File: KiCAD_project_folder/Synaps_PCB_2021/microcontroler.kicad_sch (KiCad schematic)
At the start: 27 parts, among them IC2 ESP32-S2, Y2 Crystal_GND24

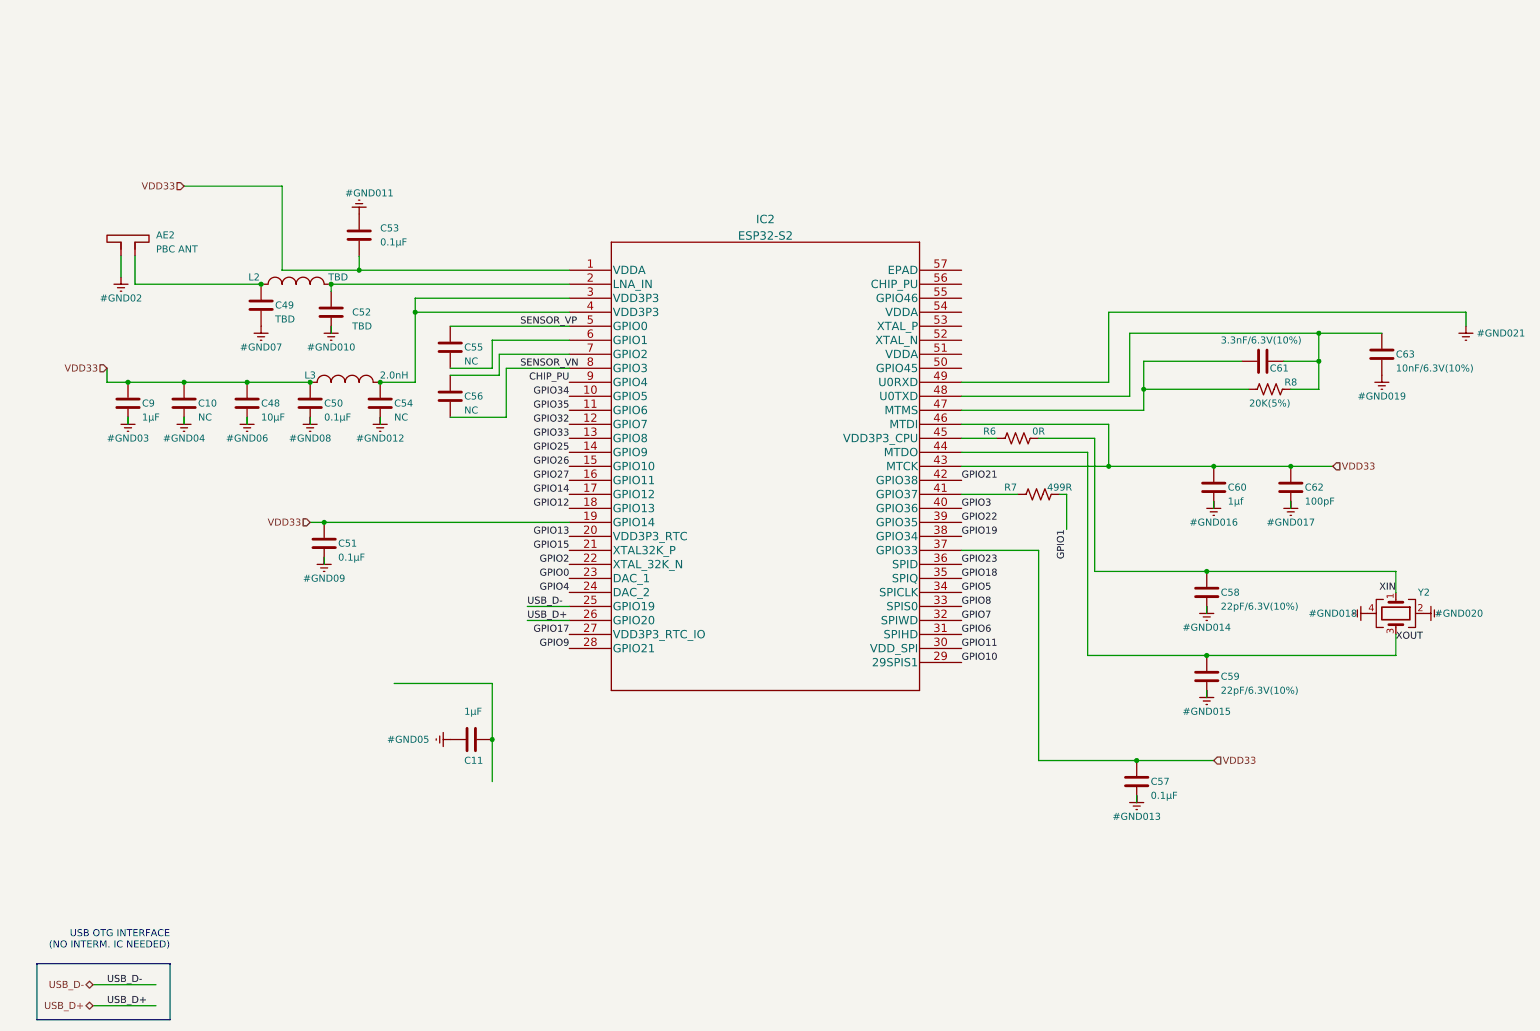
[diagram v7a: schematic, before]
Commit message: Redid schematic, fixed wrong setup
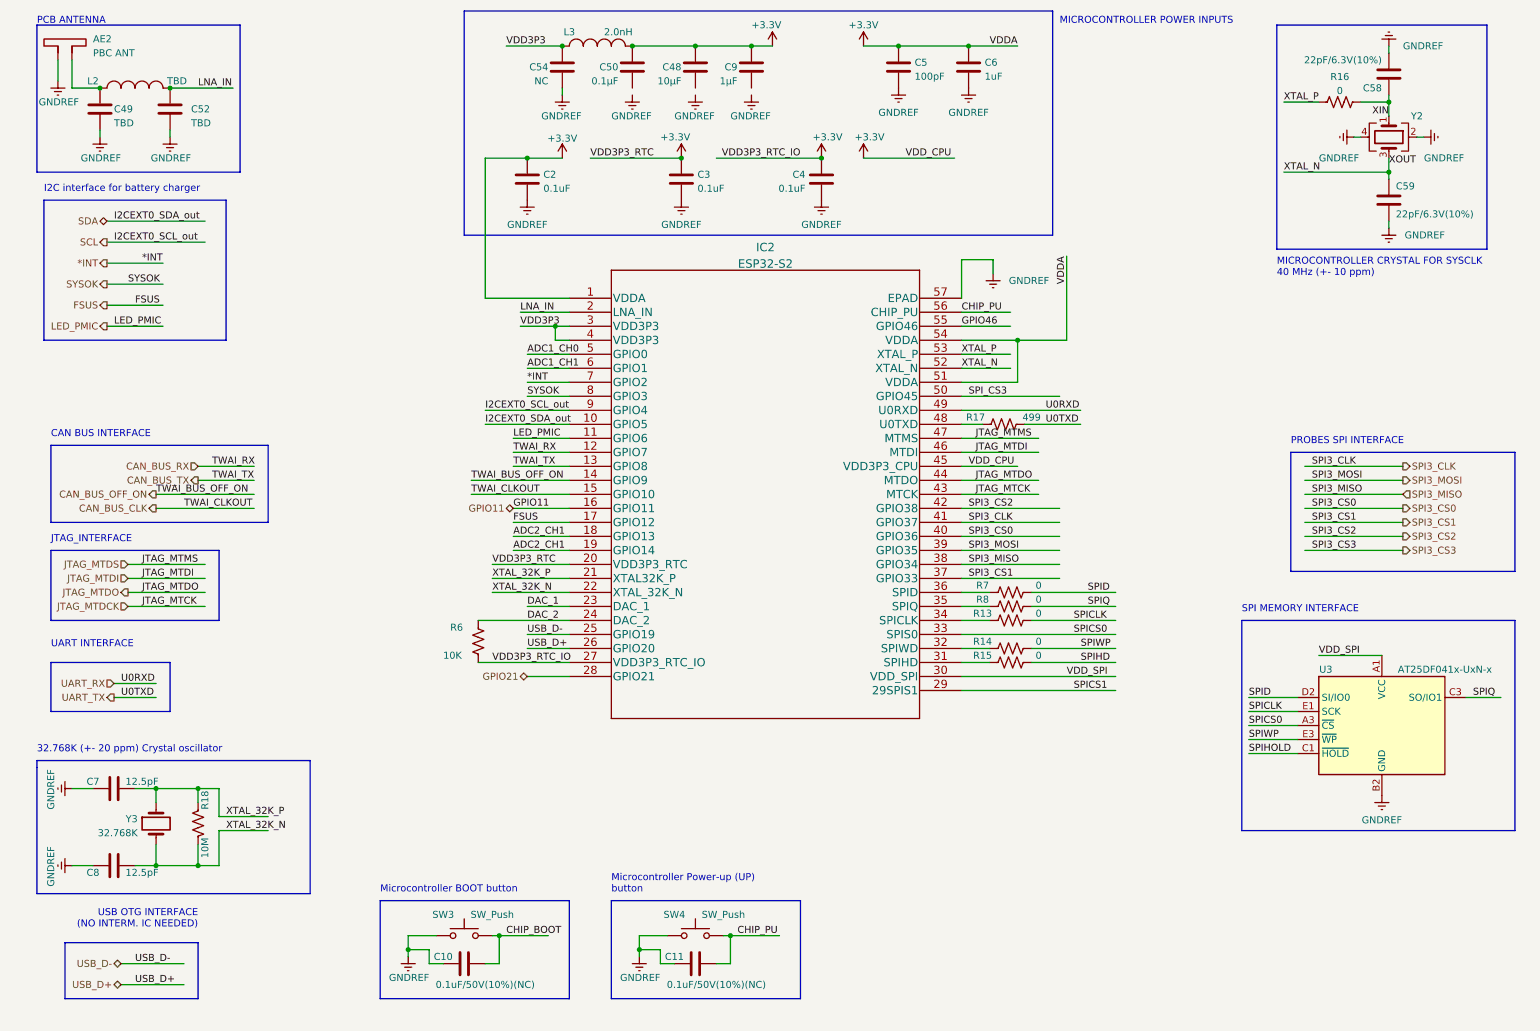
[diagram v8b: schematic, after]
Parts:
- removed C51, C53, C57: 0.1µF, Capacitor_SMD:C_1206_3216Metric_Pad1.33x1.80mm_HandSolder, symbol Device:C
- removed C55, C56: NC, Capacitor_SMD:C_1206_3216Metric_Pad1.33x1.80mm_HandSolder, symbol Device:C
- removed C60: 1µf, Capacitor_SMD:C_1206_3216Metric_Pad1.33x1.80mm_HandSolder, symbol Device:C
- removed C61: 3.3nF/6.3V(10%), Capacitor_SMD:C_1206_3216Metric_Pad1.33x1.80mm_HandSolder, symbol Device:C
- removed C62: 100pF, Capacitor_SMD:C_1206_3216Metric_Pad1.33x1.80mm_HandSolder, symbol Device:C
- removed C63: 10nF/6.3V(10%), Capacitor_SMD:C_1206_3216Metric_Pad1.33x1.80mm_HandSolder, symbol Device:C
- added C2, C3, C4: 0.1uF, symbol Device:C
- added C5: 100pF, symbol Device:C
- added C6: 1uF, symbol Device:C
- added C7, C8: 12.5pF, symbol Device:C
- added R13, R14, R15, R16: 0, symbol Device:R_US
- added R17: 499, symbol Device:R_US
- added R18: 10M, symbol Device:R_US
- added SW3, SW4: SW_Push, symbol Switch:SW_Push
- added U3: AT25DF041x-UxN-x, Package_CSP:WLCSP-8_1.58x1.63x0.35mm_Layout3x5_P0.35x0.4mm_Ball0.25mm_Pad0.25mm_NSMD, symbol Memory_Flash:AT25DF041x-UxN-x
- added Y3: 32.768K, symbol Device:Crystal
- C10: value NC -> 0.1uF/50V(10%)(NC); footprint Capacitor_SMD:C_1206_3216Metric_Pad1.33x1.80mm_HandSolder -> (none)
- C11: value 1µF -> 0.1uF/50V(10%)(NC); footprint Capacitor_SMD:C_1206_3216Metric_Pad1.33x1.80mm_HandSolder -> (none)
- R6: value 0R -> 10K; footprint Resistor_SMD:R_1206_3216Metric_Pad1.30x1.75mm_HandSolder -> (none)
- R7: value 499R -> 0; footprint Resistor_SMD:R_1206_3216Metric_Pad1.30x1.75mm_HandSolder -> (none)
- R8: value 20K(5%) -> 0; footprint Resistor_SMD:R_1206_3216Metric_Pad1.30x1.75mm_HandSolder -> (none)
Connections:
- net GPIO13 is gone; now on net +3V3: IC2.20 (VDD3P3_RTC)
- net GPIO17 is gone; now on net +3V3: IC2.27 (VDD3P3_RTC_IO)
- net GPIO18 is gone; now on an unnamed net: IC2.35 (SPIQ)
- net GPIO23 is gone; now on an unnamed net: IC2.36 (SPID)
- net GPIO27 is gone; now on net GPIO11: IC2.16 (GPIO11)
- net GPIO9 is gone; now on net GPIO21: IC2.28 (GPIO21)
- net CHIP_PU: now also C11.1, IC2.56 (CHIP_PU), SW4.2; no longer IC2.9 (GPIO4)
- net GPIO11: no longer IC2.30 (VDD_SPI)
- net GPIO21: no longer IC2.42 (GPIO38)
- net XIN: now also R16.2; no longer R6.1
- net XOUT: now also IC2.52 (XTAL_N); no longer IC2.44 (MTDO)
- net at R8.1: no longer IC2.48 (U0TXD)
- net LNA_IN: now reaches C52.1, IC2.2 (LNA_IN), L2.2
- net VDD3P3: now reaches C54.1, IC2.3 (VDD3P3), IC2.4 (VDD3P3), L3.2
- net SPI3_CLK: now reaches IC2.41 (GPIO37)
- net SPI3_CLK: no longer R7.2
- net +3V3: now reaches IC2.45 (VDD3P3_CPU), R6.2
- net +3V3: now also C48.1, C50.1, C9.1, IC2.1 (VDDA), IC2.51 (VDDA), IC2.54 (VDDA), L3.1, C2.1, C3.1, C4.1, C5.1, C6.1
- net JTAG_MTDS: now reaches IC2.47 (MTMS)
- net JTAG_MTDS: no longer R8.2
- net SPI_CS3: now reaches IC2.50 (GPIO45)
- net XTAL_P: now reaches IC2.53 (XTAL_P)
- net XTAL_P: now also R16.1
- net GPIO46: now reaches IC2.55 (GPIO46)
- net GNDREF: now reaches IC2.57 (EPAD)
- net GNDREF: now also AE2.1, C10.2, C11.2, C49.2, C52.2, C54.2, C58.2, C59.2, Y2.2, Y2.4, C2.2, C3.2, C4.2, C5.2, C6.2, C7.1, C8.1, SW3.1, SW4.1, U3.B2 (GND)
- net ADC1_CH1: now reaches IC2.6 (GPIO1)
- net *INT: now reaches IC2.7 (GPIO2)
- removed net Earth: AE2.1, C10.2, C11.2, C48.2, C49.2, C50.2, C52.2, C54.2, C58.2, C59.2, C9.2, IC2.49 (U0RXD), Y2.2, Y2.4
- net GPIO0 renamed DAC_1
- net GPIO1: no longer names the net of R7.1
- net GPIO10 renamed SPICS1
- net GPIO12 renamed ADC2_CH1
- net ADC2_CH1: now also IC2.19 (GPIO14)
- net GPIO14 renamed FSUS
- net GPIO15 renamed XTAL_32K_P
- net XTAL_32K_P: now also C7.2, R18.1, Y3.1
- net GPIO19 renamed SPI3_MISO
- net GPIO2 renamed XTAL_32K_N
- net XTAL_32K_N: now also C8.2, R18.2, Y3.2
- net GPIO22 renamed SPI3_MOSI
- net GPIO25 renamed CAN_BUS_OFF_ON
- net GPIO26 renamed CAN_BUS_CLK
- net GPIO3 renamed SPI3_CS0
- net GPIO32 renamed CAN_BUS_RX
- net GPIO33 renamed CAN_BUS_TX
- net GPIO34 renamed SDA
- net GPIO35 renamed LED_PMIC
- net GPIO4 renamed DAC_2
- net DAC_2: now also R6.1
- net GPIO5: no longer names the net of IC2.34 (SPICLK)
- net GPIO5: now also R13.1
- net GPIO6: no longer names the net of IC2.31 (SPIHD)
- net GPIO6: now also R15.1
- net GPIO7: no longer names the net of IC2.32 (SPIWD)
- net GPIO7: now also R14.1
- net GPIO8 renamed SPICS0
- net SPICS0: now also U3.A3 (~{CS})
- net SENSOR_VN renamed SYSOK
- net SENSOR_VP renamed ADC1_CH0
- removed net VDD33: C10.1, C48.1, C50.1, C9.1, IC2.1 (VDDA), IC2.19 (GPIO14), IC2.37 (GPIO33), IC2.43 (MTCK), IC2.46 (MTDI), L3.1
- new net: IC2.48 (U0TXD), R17.1
- new net CHIP_BOOT: C10.1, SW3.2
- new net JTAG_MTDCK: IC2.43 (MTCK)
- new net JTAG_MTDI: IC2.46 (MTDI)
- new net JTAG_MTDO: IC2.44 (MTDO)
- new net SCL: IC2.9 (GPIO4)
- new net SPI3_CS1: IC2.37 (GPIO33)
- new net SPI3_CS2: IC2.42 (GPIO38)
- new net SPICLK: R13.2, U3.E1 (SCK)
- new net SPID: R7.2, U3.D2 (SI/IO0)
- new net SPIHD: R15.2
- new net SPIHOLD: U3.C1 (~{HOLD})
- new net SPIQ: R8.2, U3.C3 (SO/IO1)
- new net SPIWP: R14.2, U3.E3 (~{WP})
- new net UART_RX: IC2.49 (U0RXD)
- new net UART_TX: R17.2
- new net VDD_SPI: IC2.30 (VDD_SPI), U3.A1 (VCC)
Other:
- note added: "32.768K (+- 20 ppm) Crystal oscillator"
- note added: "CAN BUS INTERFACE"
- note added: "I2C interface for battery charger"
- note added: "JTAG_INTERFACE"
- note added: "MICROCONTROLLER CRYSTAL FOR SYSCLK 40 MHz (+- 10 ppm)"
- note added: "MICROCONTROLLER POWER INPUTS"
- note added: "Microcontroller BOOT button"
- note added: "Microcontroller Power-up (UP) button"
- note added: "PCB ANTENNA"
- note added: "PROBES SPI INTERFACE"
- note added: "SPI MEMORY INTERFACE"
- note added: "UART INTERFACE"
- moved on the sheet: AE2, C48, C49, C50, C52, C54, C58, C59, C9, IC2, L2, L3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
